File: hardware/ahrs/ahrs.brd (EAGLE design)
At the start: 30 x 30 mm, 32 parts, among them J1 2-PIN, U1 LSM9DS1, U2 STM32G4_UFQFPN48_T1, X1 NX2016SA24MHZ-EXS00A-CS11335, X2 SM08B-SRSS-TB

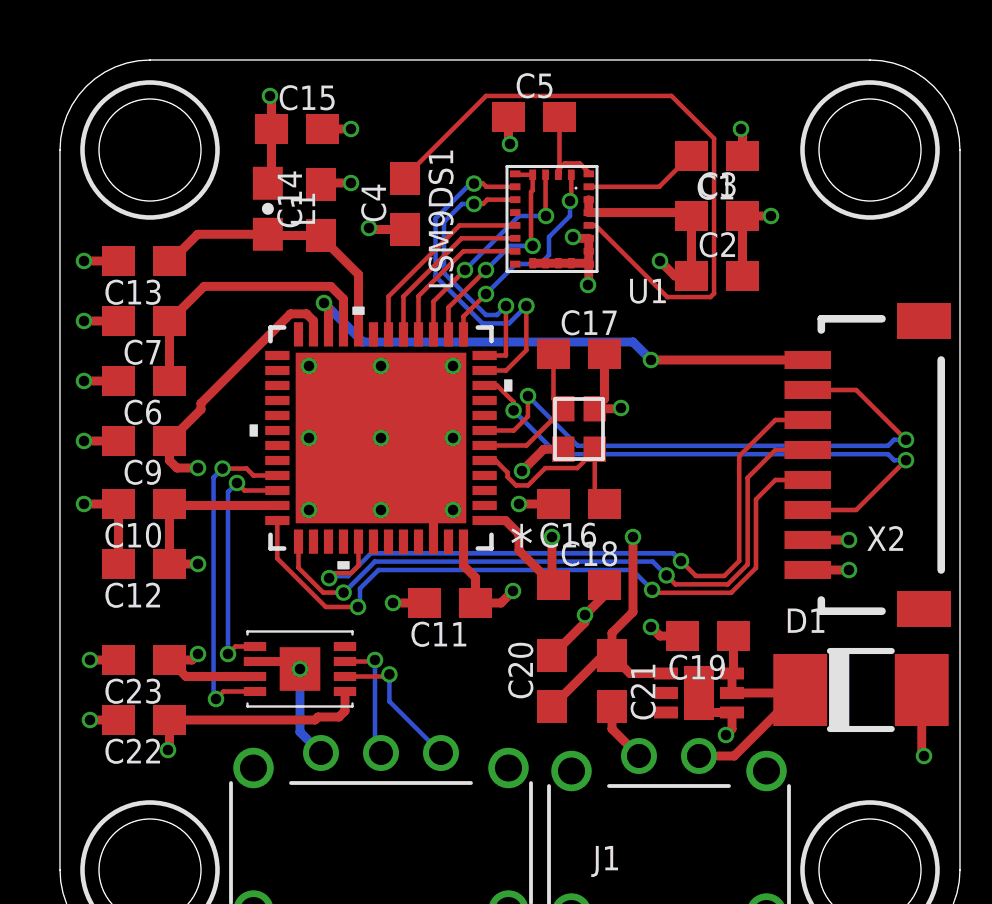
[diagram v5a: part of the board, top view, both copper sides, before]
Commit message: Lowered lpuartrx trace width
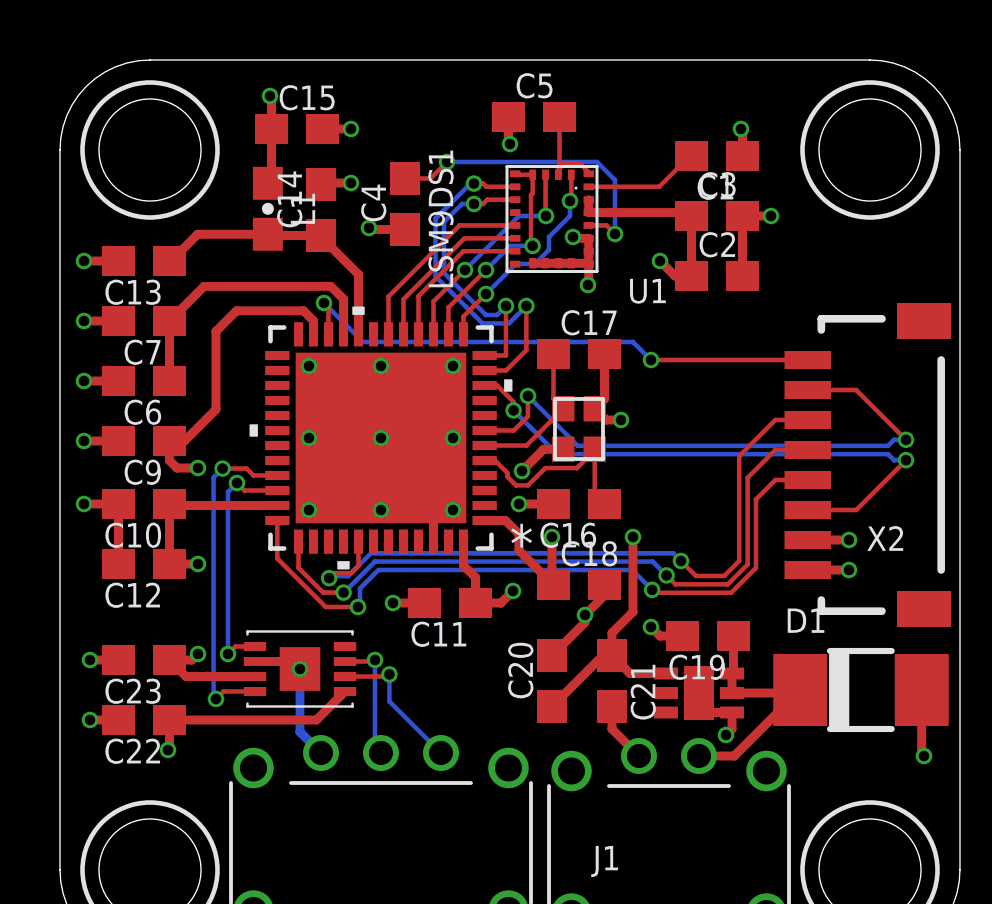
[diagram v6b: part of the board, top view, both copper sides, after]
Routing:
- net N$3: track 22.4 -> 10.3 mm, vias 0 -> 2
- net 3.3V: track 53.3 -> 54.4 mm
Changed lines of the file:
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@@
 <wire x1="17.825" y1="18.375" x2="18.15" y2="18.7" width="0.3" layer="1"/>
 <wire x1="18.15" y1="18.7" x2="18.15" y2="20.2" width="0.3" layer="1"/>
-<wire x1="17.825" y1="18.375" x2="18.675" y2="18.375" width="0.3" layer="1"/>
-<wire x1="18.675" y1="18.375" x2="18.7" y2="18.4" width="0.3" layer="1"/>
-<via x="18.7" y="18.4" extent="1-16" drill="0.35"/>
 <wire x1="16.775" y1="17.025" x2="16.125" y2="17.025" width="0.3" layer="1"/>
 <wire x1="16.125" y1="17.025" x2="15.4" y2="16.3" width="0.3" layer="1"/>
@@
 <wire x1="1.95" y1="23.3" x2="0.8" y2="23.3" width="0.3" layer="1"/>
 <via x="0.8" y="23.3" extent="1-16" drill="0.35"/>
+<wire x1="17.825" y1="18.375" x2="18.2" y2="18" width="0.3" layer="1"/>
+<wire x1="18.2" y1="18" x2="18.7" y2="18" width="0.3" layer="1"/>
+<via x="18.7" y="18" extent="1-16" drill="0.35"/>
 </signal>
 <signal name="3.3V" class="1">
@@
 <wire x1="3.65" y1="13.2" x2="4.6" y2="13.2" width="0.3" layer="1"/>
 <via x="4.6" y="13.2" extent="1-16" drill="0.35"/>
-<wire x1="9.5" y1="8.95" x2="9.5" y2="8.3" width="0.3" layer="1"/>
-<wire x1="9.5" y1="8.3" x2="9.3" y2="8.1" width="0.3" layer="1"/>
-<wire x1="9.3" y1="8.1" x2="8.6" y2="8.1" width="0.3" layer="1"/>
-<wire x1="8.5" y1="8" x2="3.65" y2="8" width="0.3" layer="1"/>
-<wire x1="8.5" y1="8" x2="8.6" y2="8.1" width="0.3" layer="1"/>
 <wire x1="3.65" y1="8" x2="3.65" y2="7.05" width="0.3" layer="1"/>
 <wire x1="3.65" y1="7.05" x2="3.6" y2="7" width="0.3" layer="1"/>
@@
 <via x="26.3" y="13" extent="1-16" drill="0.35"/>
 <wire x1="8.45" y1="20.8544" x2="8.45" y2="21.3049375" width="0.3" layer="1"/>
-<wire x1="8.45" y1="21.3049375" x2="8.2171375" y2="21.5378" width="0.3" layer="1"/>
-<wire x1="8.2171375" y1="21.5378" x2="7.6828625" y2="21.5378" width="0.3" layer="1"/>
-<wire x1="7.6828625" y1="21.5378" x2="4.7" y2="18.5549375" width="0.3" layer="1"/>
-<wire x1="4.7" y1="18.5549375" x2="4.7" y2="18.35" width="0.3" layer="1"/>
-<wire x1="4.7" y1="18.35" x2="3.65" y2="17.3" width="0.3" layer="1"/>
+<wire x1="8.45" y1="21.3049375" x2="8.1171375" y2="21.6378" width="0.3" layer="1"/>
+<wire x1="8.1171375" y1="21.6378" x2="5.8828625" y2="21.6378" width="0.3" layer="1"/>
+<wire x1="5.8828625" y1="21.6378" x2="5.2" y2="20.9549375" width="0.3" layer="1"/>
+<wire x1="5.2" y1="20.9549375" x2="5.2" y2="18.35" width="0.3" layer="1"/>
+<wire x1="5.2" y1="18.35" x2="4.15" y2="17.3" width="0.3" layer="1"/>
+<wire x1="4.15" y1="17.3" x2="3.65" y2="17.3" width="0.3" layer="1"/>
 <wire x1="13.45" y1="13.9456" x2="13.45" y2="13.15" width="0.3" layer="1"/>
 <wire x1="13.85" y1="12.75" x2="13.85" y2="11.9" width="0.3" layer="1"/>
 <wire x1="13.45" y1="13.15" x2="13.85" y2="12.75" width="0.3" layer="1"/>
+<wire x1="9.5" y1="8.95" x2="8.55" y2="8" width="0.3" layer="1"/>
+<wire x1="8.55" y1="8" x2="3.65" y2="8" width="0.3" layer="1"/>
 </signal>
 <signal name="N$2">
@@
 <contactref element="U1" pad="P$21"/>
 <contactref element="C4" pad="2"/>
-<wire x1="17.625" y1="24.485" x2="17.855" y2="24.485" width="0.1524" layer="1"/>
-<wire x1="17.855" y1="24.485" x2="20.243209375" y2="22.096790625" width="0.1524" layer="1"/>
-<wire x1="20.243209375" y1="22.096790625" x2="21.684178125" y2="22.096790625" width="0.1524" layer="1"/>
-<wire x1="21.684178125" y1="22.096790625" x2="21.803209375" y2="22.215821875" width="0.1524" layer="1"/>
-<wire x1="21.803209375" y1="22.215821875" x2="21.803209375" y2="27.384178125" width="0.1524" layer="1"/>
-<wire x1="21.803209375" y1="27.384178125" x2="20.384178125" y2="28.803209375" width="0.1524" layer="1"/>
-<wire x1="20.384178125" y1="28.803209375" x2="14.203209375" y2="28.803209375" width="0.1524" layer="1"/>
-<wire x1="14.203209375" y1="28.803209375" x2="11.5" y2="26.1" width="0.1524" layer="1"/>
-<wire x1="11.5" y1="26.1" x2="11.5" y2="26.05" width="0.1524" layer="1"/>
+<wire x1="17.625" y1="24.485" x2="18.215" y2="24.485" width="0.1524" layer="1"/>
+<wire x1="18.215" y1="24.485" x2="18.5" y2="24.2" width="0.1524" layer="1"/>
+<via x="18.5" y="24.2" extent="1-16" drill="0.35"/>
+<wire x1="18.5" y1="24.2" x2="18.5" y2="26" width="0.1524" layer="16"/>
+<wire x1="17.9" y1="26.6" x2="12.9" y2="26.6" width="0.1524" layer="16"/>
+<via x="12.9" y="26.6" extent="1-16" drill="0.35"/>
+<wire x1="12.9" y1="26.6" x2="12.35" y2="26.05" width="0.1524" layer="1"/>
+<wire x1="12.35" y1="26.05" x2="11.5" y2="26.05" width="0.1524" layer="1"/>
+<wire x1="18.5" y1="26" x2="17.9" y2="26.6" width="0.1524" layer="16"/>
 </signal>
 <signal name="N$4">
@@
 <contactref element="C16" pad="1"/>
 <contactref element="U2" pad="5"/>
-<wire x1="17.825" y1="17.025" x2="17.825" y2="16.975" width="0.1524" layer="1"/>
-<wire x1="17.825" y1="16.975" x2="17.246790625" y2="16.396790625" width="0.1524" layer="1"/>
-<wire x1="14.5161625" y1="16.65" x2="14.1544" y2="16.65" width="0.1524" layer="1"/>
 <wire x1="18.15" y1="15.2" x2="17.825" y2="15.525" width="0.1524" layer="1"/>
 <wire x1="17.825" y1="15.525" x2="17.825" y2="17.025" width="0.1524" layer="1"/>
 <wire x1="15.59874375" y1="15.8202" x2="15.20125625" y2="15.8202" width="0.1524" layer="1"/>
 <wire x1="15.20125625" y1="15.8202" x2="14.9202" y2="16.10125625" width="0.1524" layer="1"/>
-<wire x1="14.9202" y1="16.10125625" x2="14.9202" y2="16.2459625" width="0.1524" layer="1"/>
-<wire x1="17.246790625" y1="16.396790625" x2="16.175334375" y2="16.396790625" width="0.1524" layer="1"/>
 <wire x1="16.175334375" y1="16.396790625" x2="15.59874375" y2="15.8202" width="0.1524" layer="1"/>
-<wire x1="14.9202" y1="16.2459625" x2="14.5161625" y2="16.65" width="0.1524" layer="1"/>
+<wire x1="17.825" y1="17.025" x2="17.825" y2="16.98763125" width="0.1524" layer="1"/>
+<wire x1="17.825" y1="16.98763125" x2="17.234159375" y2="16.396790625" width="0.1524" layer="1"/>
+<wire x1="17.234159375" y1="16.396790625" x2="16.175334375" y2="16.396790625" width="0.1524" layer="1"/>
+<wire x1="14.9202" y1="16.10125625" x2="14.9202" y2="16.23036875" width="0.1524" layer="1"/>
+<wire x1="14.9202" y1="16.23036875" x2="14.50056875" y2="16.65" width="0.1524" layer="1"/>
+<wire x1="14.50056875" y1="16.65" x2="14.1544" y2="16.65" width="0.1524" layer="1"/>
 </signal>
 <signal name="5V" class="1">
@@
 <via x="15.7536" y="23.8036" extent="1-16" drill="0.35"/>
 <wire x1="15.7536" y1="23.8036" x2="15.7" y2="23.8572" width="0.1524" layer="1"/>
-<wire x1="15.7" y1="23.8572" x2="15.7" y2="25.6" width="0.1524" layer="1"/>
-<wire x1="15.7" y1="25.6" x2="15.755" y2="25.655" width="0.1524" layer="1"/>
-<wire x1="15.755" y1="25.655" x2="15.755" y2="26.175" width="0.1524" layer="1"/>
+<wire x1="15.7" y1="23.8572" x2="15.7" y2="25.5" width="0.1524" layer="1"/>
+<wire x1="15.7" y1="25.5" x2="15.755" y2="25.555" width="0.1524" layer="1"/>
+<wire x1="15.755" y1="25.555" x2="15.755" y2="26.175" width="0.1524" layer="1"/>
 </signal>
 <signal name="CS_AG">
@@
 <contactref element="U2" pad="13"/>
 <wire x1="13.45" y1="20.8544" x2="13.45" y2="21.45" width="0.1524" layer="1"/>
-<wire x1="13.45" y1="21.45" x2="14.2" y2="22.2" width="0.1524" layer="1"/>
+<wire x1="13.45" y1="21.45" x2="13.8" y2="21.8" width="0.1524" layer="1"/>
 <via x="14.2" y="22.2" extent="1-16" drill="0.35"/>
+<wire x1="13.8" y1="21.8" x2="14.2" y2="22.2" width="0.1524" layer="1"/>
 <wire x1="14.2" y1="22.2" x2="15.2" y2="23.2" width="0.1524" layer="16"/>
-<wire x1="15.2" y1="23.2" x2="16" y2="23.2" width="0.1524" layer="16"/>
-<wire x1="16" y1="23.2" x2="16.3" y2="23.5" width="0.1524" layer="16"/>
 <wire x1="16.3" y1="24.1" x2="17" y2="24.8" width="0.1524" layer="16"/>
 <wire x1="17" y1="24.8" x2="17" y2="25.3" width="0.1524" layer="16"/>
@@
 <wire x1="17" y1="25.3" x2="17.045" y2="25.345" width="0.1524" layer="1"/>
 <wire x1="17.045" y1="25.345" x2="17.045" y2="26.175" width="0.1524" layer="1"/>
-<wire x1="16.3" y1="23.5" x2="16.3" y2="24.1" width="0.1524" layer="16"/>
+<wire x1="15.2" y1="23.2" x2="15.82854375" y2="23.2" width="0.1524" layer="16"/>
+<wire x1="15.82854375" y1="23.2" x2="16.3" y2="23.67145625" width="0.1524" layer="16"/>
+<wire x1="16.3" y1="23.67145625" x2="16.3" y2="24.1" width="0.1524" layer="16"/>
 </signal>
 <signal name="INT_M">
@@
 <contactref element="U1" pad="P$11"/>
 <contactref element="U2" pad="17"/>
-<wire x1="15.175" y1="24.055" x2="13.3888375" y2="24.055" width="0.1524" layer="1"/>
-<wire x1="13.3888375" y1="24.055" x2="11.45" y2="22.1161625" width="0.1524" layer="1"/>
-<wire x1="11.45" y1="22.1161625" x2="11.45" y2="20.8544" width="0.1524" layer="1"/>
+<wire x1="15.175" y1="24.055" x2="13.48131875" y2="24.055" width="0.1524" layer="1"/>
+<wire x1="13.48131875" y1="24.055" x2="11.45" y2="22.02368125" width="0.1524" layer="1"/>
+<wire x1="11.45" y1="22.02368125" x2="11.45" y2="20.8544" width="0.1524" layer="1"/>
 </signal>
 <signal name="INT2_AG">
@@
 <contactref element="U2" pad="22"/>
 <contactref element="X2" pad="8"/>
-<wire x1="24.925" y1="20" x2="19.7" y2="20" width="0.3" layer="1"/>
+<wire x1="24.925" y1="20" x2="19.7" y2="20" width="0.1524" layer="1"/>
 <via x="19.7" y="20" extent="1-16" drill="0.35"/>
-<wire x1="19.7" y1="20" x2="19.1" y2="20.6" width="0.3" layer="16"/>
-<wire x1="19.1" y1="20.6" x2="10.1" y2="20.6" width="0.3" layer="16"/>
-<wire x1="10.1" y1="20.6" x2="8.8" y2="21.9" width="0.3" layer="16"/>
+<wire x1="19.7" y1="20" x2="19.1" y2="20.6" width="0.1524" layer="16"/>
+<wire x1="19.1" y1="20.6" x2="10.1" y2="20.6" width="0.1524" layer="16"/>
+<wire x1="10.1" y1="20.6" x2="8.8" y2="21.9" width="0.1524" layer="16"/>
 <via x="8.8" y="21.9" extent="1-16" drill="0.35"/>
-<wire x1="8.8" y1="21.9" x2="8.95" y2="21.75" width="0.3" layer="1"/>
-<wire x1="8.95" y1="21.75" x2="8.95" y2="20.8544" width="0.3" layer="1"/>
+<wire x1="8.8" y1="21.9" x2="8.95" y2="21.75" width="0.1524" layer="1"/>
+<wire x1="8.95" y1="21.75" x2="8.95" y2="20.8544" width="0.1524" layer="1"/>
 </signal>
 <signal name="LPUART_TX">

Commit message: Pre logo
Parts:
- removed U$1: LDFM33PUR, timlib:DFN6_2X2
- removed U$3: MCP2542FD, timlib:TDFN_2X3
- removed U$5: 3-PIN, timlib:M80-8430342
- removed X2: SM08B-SRSS-TB, timlib:SM08B-SRSS-TB
- added D2: LED_0603150060RS75000, timlib:D0603
- added H1, H2, H3, H4: GND_HOLE_M3, timlib:HOLE_GND_M3
- added J2: 3-PIN3, timlib:M80-8430342
- added J3: SM08B-SRSS-TB, timlib:SM08B-SRSS-TB
- added R1: 68, rcl:R0603
- added U3: LDFM33PUR, timlib:DFN6_2X2
- added U4: MCP2542FD, timlib:TDFN_2X3
- moved C4 9.18 mm to (20.3, 22.6)
- moved C5 5.35 mm to (20.8, 26.2), turned to 180 degrees
- moved C1 2.42 mm to (24.0, 25.6)
- moved C2 2.28 mm to (24.0, 21.9)
- moved C3 2.28 mm to (24.0, 23.9)
- moved C10 1.00 mm to (3.80, 15.2)
- moved C11 1.00 mm to (14.0, 11.9)
- moved C12 1.00 mm to (3.80, 13.2)
- moved C13 1.00 mm to (3.80, 23.3)
- moved C14 1.00 mm to (9.70, 25.0)
- moved C15 1.00 mm to (8.90, 27.7)
- moved C16 1.00 mm to (18.3, 15.2)
- moved C17 1.00 mm to (18.3, 20.2)
- moved C18 1.00 mm to (18.3, 12.5)
- moved C19 1.00 mm to (22.6, 10.8)
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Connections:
- new net N$1: D2.1, R1.2
- net 3.3V: now also D2.2, J3.1, U3.PIN1, U4.5; no longer U$1.PIN1, U$3.5, X2.1
- net 5V: now also U3.PIN5, U3.PIN6, U4.3; no longer U$1.PIN5, U$1.PIN6, U$3.3
- net CAN_H: now also J2.2, U4.7; no longer U$3.7, U$5.2
- net CAN_L: now also J2.1, U4.6; no longer U$3.6, U$5.1
- net CAN_RX: now also U4.4; no longer U$3.4
- net CAN_TX: now also U4.1; no longer U$3.1
- net GND: now also H1.P$1, H2.P$1, H3.P$1, H4.P$1, J2.3, J3.2, R1.1, U3.PAD, U3.PIN4, U4.2, U4.PAD; no longer U$1.PAD, U$1.PIN4, U$3.2, U$3.PAD, U$5.3, X2.2
- net LPUART_RX: now also J3.8; no longer X2.8
- net LPUART_TX: now also J3.3; no longer X2.3
- net NRST: now also J3.7; no longer X2.7
- net SWCLK: now also J3.5; no longer X2.5
- net SWDIO: now also J3.4; no longer X2.4
- net SWO: now also J3.6; no longer X2.6
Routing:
- net N$1: track 0.00 -> 12.4 mm, vias 0 -> 2
- net 3.3V: track 54.4 -> 63.1 mm, vias 10 -> 12
- net N$3: track 10.3 -> 2.54 mm, vias 2 -> 0
- net SCK: track 7.18 -> 12.5 mm, vias 2 -> 3
- net CS_M: track 9.51 -> 14.4 mm, vias 2 -> 3
- net CS_AG: track 12.2 -> 16.5 mm, vias 2 -> 3
- net MOSI: track 7.41 -> 10.9 mm, vias 2 -> 3
- net MISO: track 7.56 -> 9.97 mm, vias 2 -> 3
- net GND: track 48.9 -> 47.2 mm, vias 33 -> 34
- net SWO: track 22.8 -> 23.7 mm
- net SWDIO: track 23.7 -> 24.6 mm
- net LPUART_TX: track 19.2 -> 18.3 mm
- net LPUART_RX: track 18.0 -> 18.9 mm
- net NRST: track 19.7 -> 18.8 mm
- net SWCLK: track 22.5 -> 23.4 mm
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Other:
- board size 30 x 30 mm -> 32 x 30 mm
- board text added: "5V"
- board text added: "CS_AG"
- board text added: "CS_M"
- board text added: "GND"
- board text added: "MISO"
- board text added: "MOSI"
- board text added: "SCK"
